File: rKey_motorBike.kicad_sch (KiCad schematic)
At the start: 5 parts

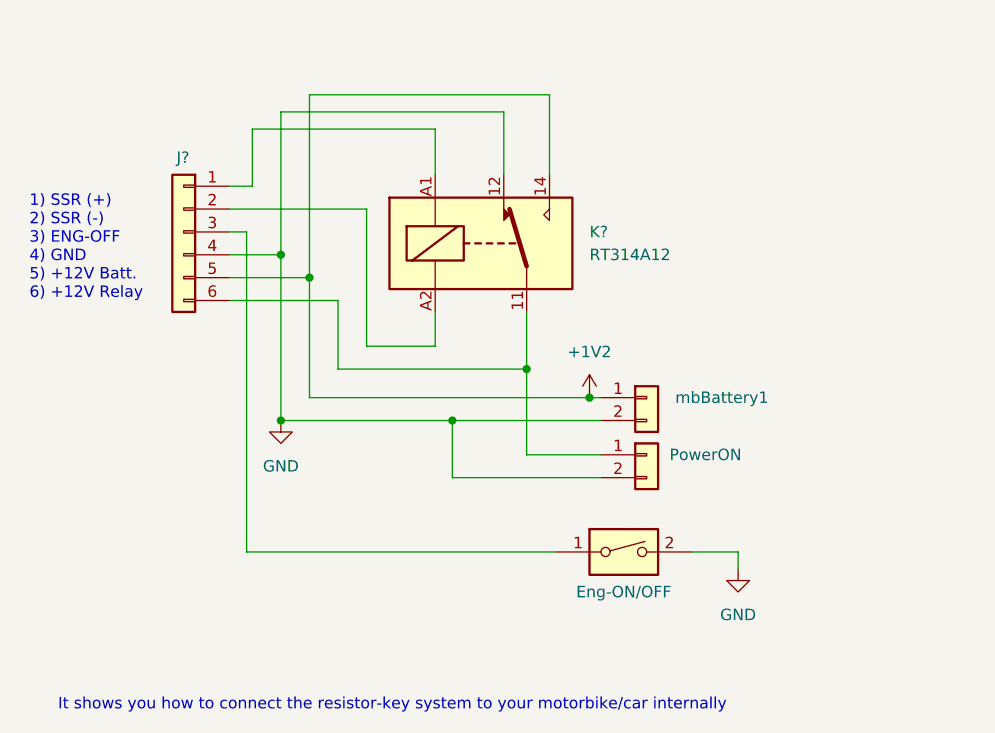
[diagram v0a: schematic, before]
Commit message: Fix: engine stop button missing
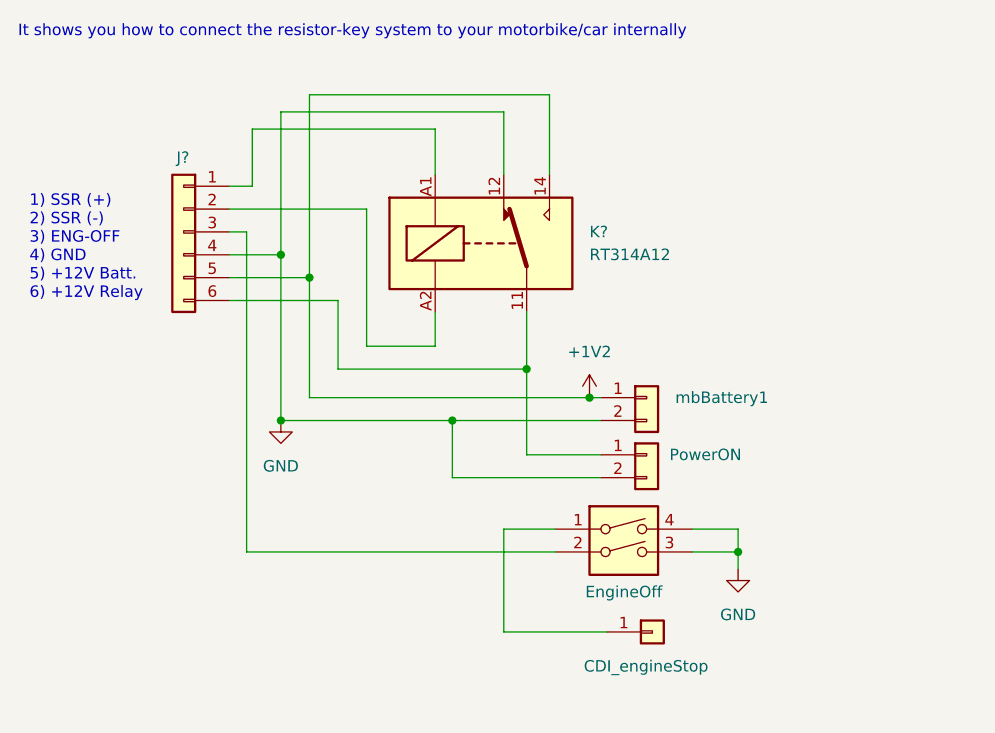
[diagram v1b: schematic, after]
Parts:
- removed Eng-ON/OFF: SW_DIP_x01, symbol Switch:SW_DIP_x01
- added CDI_engineStop: Conn_01x01, symbol Connector_Generic:Conn_01x01
- added EngineOff: SW_DIP_x02, symbol Switch:SW_DIP_x02
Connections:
- net GND: now also EngineOff.3, EngineOff.4
- net at J?.3 (Pin_3): now also EngineOff.2
- new net: CDI_engineStop.1 (Pin_1), EngineOff.1
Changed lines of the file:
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@@
   (junction (at 128.905 67.945) (diameter 0) (color 0 0 0 0)
   )
+  (junction (at 176.53 98.425) (diameter 0) (color 0 0 0 0)
+  )
   (junction (at 125.73 83.82) (diameter 0) (color 0 0 0 0)
   )
@@
     (stroke (width 0) (type default) (color 0 0 0 0))
   )
+  (wire (pts (xy 176.53 95.885) (xy 176.53 98.425))
+    (stroke (width 0) (type default) (color 0 0 0 0))
+  )
   (wire (pts (xy 128.905 67.945) (xy 120.015 67.945))
     (stroke (width 0) (type default) (color 0 0 0 0))
   )
+  (wire (pts (xy 171.45 95.885) (xy 176.53 95.885))
+    (stroke (width 0) (type default) (color 0 0 0 0))
+  )
   (wire (pts (xy 171.45 98.425) (xy 176.53 98.425))
     (stroke (width 0) (type default) (color 0 0 0 0))
@@
     (stroke (width 0) (type default) (color 0 0 0 0))
   )
+  (wire (pts (xy 156.21 95.885) (xy 150.495 95.885))
+    (stroke (width 0) (type default) (color 0 0 0 0))
+  )
   (wire (pts (xy 128.905 67.945) (xy 128.905 47.625))
     (stroke (width 0) (type default) (color 0 0 0 0))
@@
     (stroke (width 0) (type default) (color 0 0 0 0))
   )
+  (wire (pts (xy 150.495 107.315) (xy 161.925 107.315))
+    (stroke (width 0) (type default) (color 0 0 0 0))
+  )
   (wire (pts (xy 160.02 81.28) (xy 128.905 81.28))
     (stroke (width 0) (type default) (color 0 0 0 0))
@@
   )
   (wire (pts (xy 144.78 90.17) (xy 144.78 83.82))
+    (stroke (width 0) (type default) (color 0 0 0 0))
+  )
+  (wire (pts (xy 150.495 95.885) (xy 150.495 107.315))
     (stroke (width 0) (type default) (color 0 0 0 0))
   )
@@
   )
   (text "It shows you how to connect the resistor-key system to your motorbike/car internally"
-    (at 100.965 116.205 0)
+    (at 96.52 41.402 0)
     (effects (font (size 1.27 1.27)) (justify left bottom))
+  )
+  (symbol (lib_id "Connector_Generic:Conn_01x01") (at 167.005 107.315 0) (unit 1)
+    (in_bom yes) (on_board yes)
+    (property "Reference" "CDI_engineStop" (id 0) (at 159.385 111.125 0)
+      (effects (font (size 1.27 1.27)) (justify left))
+    )
+    (property "Value" "Conn_01x01" (id 1) (at 170.18 108.5849 0)
+      (effects (font (size 1.27 1.27)) (justify left) hide)
+    )
+    (property "Footprint" "" (id 2) (at 167.005 107.315 0)
+      (effects (font (size 1.27 1.27)) hide)
+    )
+    (property "Datasheet" "~" (id 3) (at 167.005 107.315 0)
+      (effects (font (size 1.27 1.27)) hide)
+    )
+    (pin "1")
   )
   (symbol (lib_id "power:GND") (at 176.53 100.33 0) (unit 1)
@@
     (pin "2")
   )
-  (symbol (lib_id "Switch:SW_DIP_x01") (at 163.83 98.425 0) (unit 1)
+  (symbol (lib_id "Switch:SW_DIP_x02") (at 163.83 98.425 0) (unit 1)
     (in_bom yes) (on_board yes)
-    (property "Reference" "Eng-ON/OFF" (id 0) (at 163.83 102.87 0))
-    (property "Value" "SW_DIP_x01" (id 1) (at 163.83 92.71 0)
+    (property "Reference" "EngineOff" (id 0) (at 163.83 102.87 0))
+    (property "Value" "SW_DIP_x02" (id 1) (at 163.83 90.805 0)
       (effects (font (size 1.27 1.27)) hide)
     )
@@
     (pin "1")
     (pin "2")
+    (pin "3")
+    (pin "4")
   )
   (sheet_instances
@@
       (reference "#PWR?") (unit 1) (value "GND") (footprint "")
     )
-    (path "/c543be33-bc12-481a-a5fb-a8e77dfb9621"
-      (reference "Eng-ON/OFF") (unit 1) (value "SW_DIP_x01") (footprint "")
+    (path "/0a7a9d71-540b-49a3-92d3-60f7f0d5bb6f"
+      (reference "CDI_engineStop") (unit 1) (value "Conn_01x01") (footprint "")
+    )
+    (path "/fc306548-a306-4d8f-8cb5-55466f7f0049"
+      (reference "EngineOff") (unit 1) (value "SW_DIP_x02") (footprint "")
     )
     (path "/85e7e94e-efc4-40bb-817b-747759a19aac"
